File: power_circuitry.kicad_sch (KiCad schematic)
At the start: 13 parts, among them J1 Power_Input, Q1 SI3127DV-T1-GE3, U1 AP63203WU-7

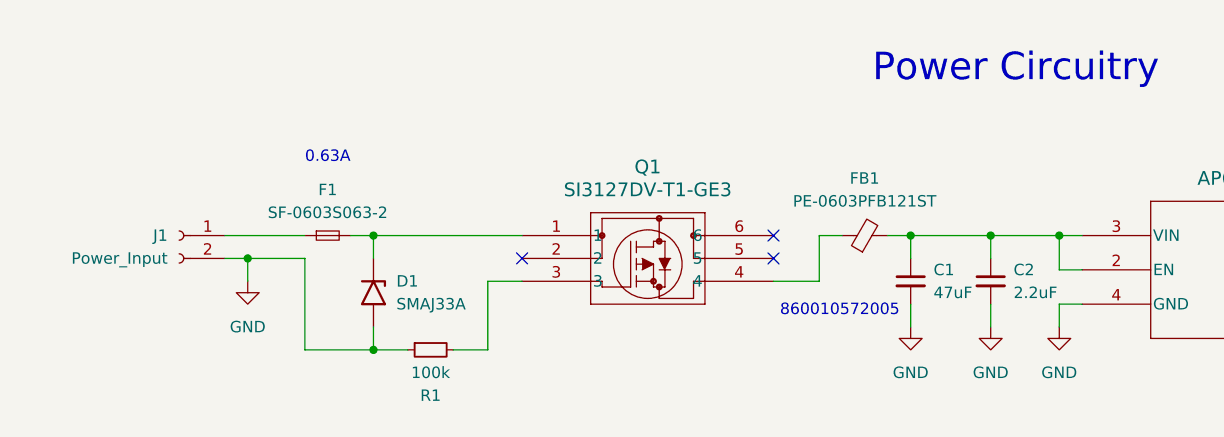
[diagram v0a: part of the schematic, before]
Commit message: rev 2 added usb prog and i2c level shifting
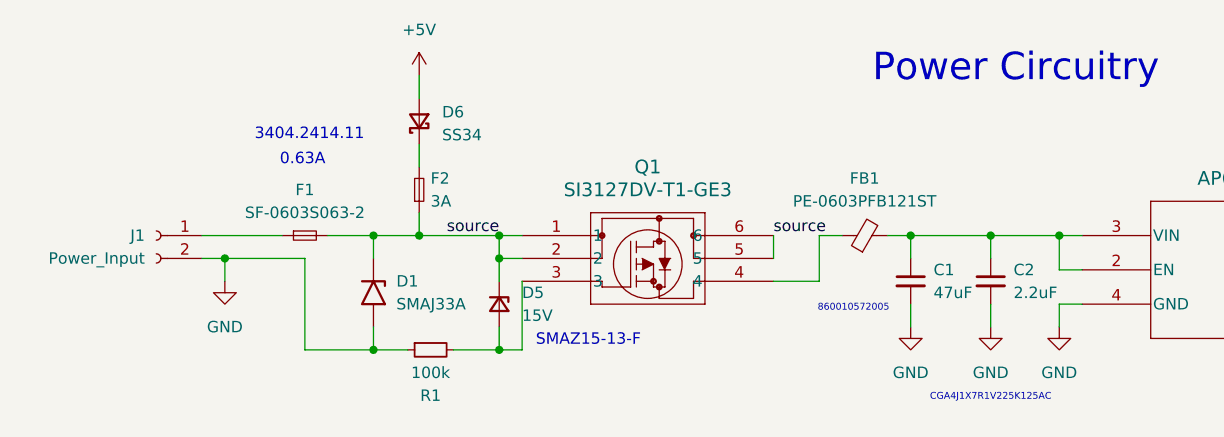
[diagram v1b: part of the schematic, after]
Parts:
- added D5: 15V, footprints:DIOM5226X240N, symbol Device:D_Zener_Small
- added D6: SS34, footprints:DIO_SS34, symbol Device:D_Schottky_Small
- added F2: 3A, Fuse:Fuse_0603_1608Metric_Pad1.05x0.95mm_HandSolder, symbol Device:Fuse_Small
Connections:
- net at Q1.3, R1.2: now also D5.2 (A)
- net source: now reaches D1.1 (A1), F1.2, Q1.1
- net source: now also Q1.2, Q1.5, Q1.6, D5.1 (K), F2.1
- new net: D6.1 (K), F2.2
- new net +5V: D6.2 (A)
- no-connect marks 3 -> 0
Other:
- note added: "3404.2414.11"
- note added: "CGA4J1X7R1V225K125AC"
- note added: "SMAZ15-13-F"
- moved on the sheet: F1, J1

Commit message: minor fixes and updated PCB layout
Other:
- note added: "SWAP"
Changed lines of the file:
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@@
+		)
+	)
+	(text "SWAP\n"
+		(exclude_from_sim no)
+		(at 88.9 67.564 0)
+		(effects
+			(font
+				(size 1.27 1.27)
+			)
 		)
 	)

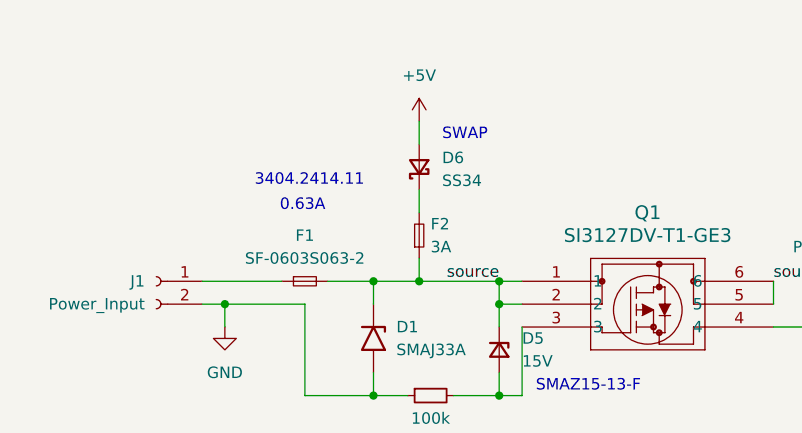
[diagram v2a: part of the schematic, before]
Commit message: Updated Schematic and fixed some routing issues
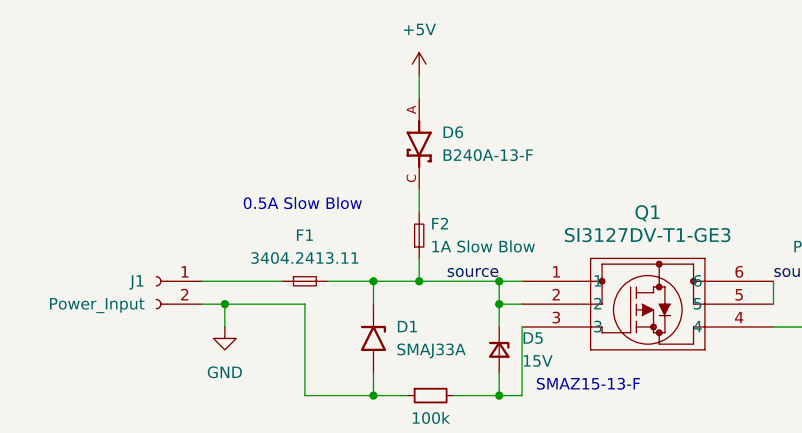
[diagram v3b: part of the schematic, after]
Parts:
- removed D6: SS34, footprints:DIO_SS34, symbol Device:D_Schottky_Small
- added D6: B240A-13-F, footprints:DIOM5226X230N, symbol B240A-13-F:B240A-13-F
- F1: value SF-0603S063-2 -> 3404.2413.11; footprint Fuse:Fuse_0603_1608Metric_Pad1.05x0.95mm_HandSolder -> footprints:Small_SMD_Fuse_Holder
- F2: value 3A -> 1A Slow Blow
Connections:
- net +5V: now also D6.A
- net at F2.2: now also D6.C
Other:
- note added: "0.5A Slow Blow"
- note removed: "0.63A"
- note removed: "3404.2414.11"
- note removed: "SWAP"
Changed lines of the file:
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@@
 	(wire
 		(pts
-			(xy 83.82 66.04) (xy 83.82 68.58)
+			(xy 83.82 60.96) (xy 83.82 63.5)
 		)
 		(stroke
@@
 		)
 	)
-	(text "SWAP\n"
-		(exclude_from_sim no)
-		(at 88.9 67.564 0)
-		(effects
-			(font
-				(size 1.27 1.27)
-			)
-		)
-	)
-	(text "0.63A"
+	(text "0.5A Slow Blow"
 		(exclude_from_sim no)
 		(at 70.866 75.438 0)
@@
 		)
 	)
-	(text "3404.2414.11\n"
-		(exclude_from_sim no)
-		(at 77.724 72.644 0)
-		(effects
-			(font
-				(size 1.27 1.27)
-			)
-			(justify right)
-		)
-	)
 	(text "Power Circuitry"
 		(exclude_from_sim no)
@@
 	)
 	(symbol
+		(lib_id "B240A-13-F:B240A-13-F")
+		(at 83.82 68.58 270)
+		(unit 1)
+		(exclude_from_sim no)
+		(in_bom yes)
+		(on_board yes)
+		(dnp no)
+		(fields_autoplaced yes)
+		(property "Reference" "D6"
+			(at 86.36 67.3099 90)
+			(effects
+				(font
+					(size 1.27 1.27)
+				)
+				(justify left)
+			)
+		)
+		(property "Value" "B240A-13-F"
+			(at 86.36 69.8499 90)
+			(effects
+				(font
+					(size 1.27 1.27)
+				)
+				(justify left)
+			)
+		)
+		(property "Footprint" "footprints:DIOM5226X230N"
+			(at 83.82 68.58 0)
+			(effects
+				(font
+					(size 1.27 1.27)
+				)
+				(justify bottom)
+				(hide yes)
+			)
+		)
+		(property "Datasheet" ""
+			(at 83.82 68.58 0)
+			(effects
+				(font
+					(size 1.27 1.27)
+				)
+				(hide yes)
+			)
+		)
+		(property "Description" ""
+			(at 83.82 68.58 0)
+			(effects
+				(font
+					(size 1.27 1.27)
+				)
+				(hide yes)
+			)
+		)
+		(property "PARTREV" "22 - 2"
+			(at 83.82 68.58 0)
+			(effects
+				(font
+					(size 1.27 1.27)
+				)
+				(justify bottom)
+				(hide yes)
+			)
+		)
+		(property "STANDARD" "IPC-7351B"
+			(at 83.82 68.58 0)
+			(effects
+				(font
+					(size 1.27 1.27)
+				)
+				(justify bottom)
+				(hide yes)
+			)
+		)
+		(property "MAXIMUM_PACKAGE_HEIGHT" "2.3 mm"
+			(at 83.82 68.58 0)
+			(effects
+				(font
+					(size 1.27 1.27)
+				)
+				(justify bottom)
+				(hide yes)
+			)
+		)
+		(property "MANUFACTURER" "Diodes"
+			(at 83.82 68.58 0)
+			(effects
+				(font
+					(size 1.27 1.27)
+				)
+				(justify bottom)
+				(hide yes)
+			)
+		)
+		(pin "C"
+		)
+		(pin "A"
+		)
+		(instances
+			(project ""
+				(path "/1b613237-19dc-4add-b759-22dbb1a2d9dd/6bdcb20a-d0aa-4381-88e7-e02725f99672"
+					(reference "D6")
+					(unit 1)
+				)
+			)
+		)
+	)
+	(symbol
 		(lib_id "Device:R_Small")
 		(at 85.09 96.52 90)
@@
 			)
 		)
-		(property "Value" "SF-0603S063-2"
+		(property "Value" "3404.2413.11"
 			(at 71.12 81.28 0)
 			(effects
@@
 			)
 		)
-		(property "Footprint" "Fuse:Fuse_0603_1608Metric_Pad1.05x0.95mm_HandSolder"
+		(property "Footprint" "footprints:Small_SMD_Fuse_Holder"
 			(at 71.12 83.82 0)
 			(effects
@@
 			)
 		)
-		(property "Value" "3A"
+		(property "Value" "1A Slow Blow"
 			(at 85.09 80.0099 90)
 			(effects
@@
 	)
 	(symbol
-		(lib_id "Device:D_Schottky_Small")
-		(at 83.82 71.12 90)
-		(unit 1)
-		(exclude_from_sim no)
-		(in_bom yes)
-		(on_board yes)
-		(dnp no)
-		(property "Reference" "D6"
-			(at 86.36 70.1039 90)
-			(effects
-				(font
-					(size 1.27 1.27)
-				)
-				(justify right)
-			)
-		)
-		(property "Value" "SS34"
-			(at 86.36 72.6439 90)
-			(effects
-				(font
-					(size 1.27 1.27)
-				)
-				(justify right)
-			)
-		)
-		(property "Footprint" "footprints:DIO_SS34"
-			(at 83.82 71.12 90)
-			(effects
-				(font
-					(size 1.27 1.27)
-				)
-				(hide yes)
-			)
-		)
-		(property "Datasheet" "~"
-			(at 83.82 71.12 90)
-			(effects
-				(font
-					(size 1.27 1.27)
-				)
-				(hide yes)
-			)
-		)
-		(property "Description" "Schottky diode, small symbol"
-			(at 83.82 71.12 0)
-			(effects
-				(font
-					(size 1.27 1.27)
-				)
-				(hide yes)
-			)
-		)
-		(pin "2"
-		)
-		(pin "1"
-		)
-		(instances
-			(project ""
-				(path "/1b613237-19dc-4add-b759-22dbb1a2d9dd/6bdcb20a-d0aa-4381-88e7-e02725f99672"
-					(reference "D6")
-					(unit 1)
-				)
-			)
-		)
-	)
-	(symbol
 		(lib_id "2025-11-24_21-08-57:AP63203WU-7")
 		(at 157.48 85.09 0)
@@
 	(symbol
 		(lib_id "power:+5V")
-		(at 83.82 66.04 0)
+		(at 83.82 60.96 0)
 		(unit 1)
 		(exclude_from_sim no)
@@
 		(fields_autoplaced yes)
 		(property "Reference" "#PWR051"
-			(at 83.82 69.85 0)
+			(at 83.82 64.77 0)
 			(effects
 				(font
@@
 		)
 		(property "Value" "+5V"
+			(at 83.82 55.88 0)
+			(effects
+				(font
+					(size 1.27 1.27)
+				)
+			)
+		)
+		(property "Footprint" ""
 			(at 83.82 60.96 0)
 			(effects
@@
 					(size 1.27 1.27)
 				)
-			)
-		)
-		(property "Footprint" ""
-			(at 83.82 66.04 0)
-			(effects
-				(font
-					(size 1.27 1.27)
-				)
 				(hide yes)
 			)
 		)
 		(property "Datasheet" ""
-			(at 83.82 66.04 0)
+			(at 83.82 60.96 0)
 			(effects
 				(font
@@
 		)
 		(property "Description" "Power symbol creates a global label with name \"+5V\""
-			(at 83.82 66.04 0)
-			(effects
-				(font
+			(at 83.82 60.96 0)
+			(effects
+				(font

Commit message: Rev A PCB Ordered
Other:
- note added: "VLS6045EX-3R9M"
- company: (none) -> FrostByte Solutions
- title: (none) -> FrostByte IR Camera Interface Board
- moved on the sheet: C1, C2, C3, C4, C5, D1, D5, D6, F1, F2, FB1, J1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
